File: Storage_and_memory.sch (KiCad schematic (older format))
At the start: 19 parts, among them J4 DM3AT-SF-PEJM5, U14 SN74AVCA406DGGR, U15 W25Q256JVFIQ

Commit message: minor changes
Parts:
- R19, R20, R21, R22: footprint Resistor_SMD:R_0805_2012Metric_Pad1.20x1.40mm_HandSolder -> Resistor_SMD:R_0805_2012Metric
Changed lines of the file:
@@
 F 0 "R19" V 4650 6430 50  0000 C CNN
 F 1 "33" V 4660 6810 50  0000 C CNN
-F 2 "Resistor_SMD:R_0805_2012Metric_Pad1.20x1.40mm_HandSolder" V 4630 6610 50  0001 C CNN
+F 2 "Resistor_SMD:R_0805_2012Metric" V 4630 6610 50  0001 C CNN
 F 3 "~" H 4700 6610 50  0001 C CNN
 F 4 "RC0805FR-0733RL" V 4700 6610 50  0001 C CNN "Type"
@@
 F 0 "R20" V 4660 6530 50  0000 C CNN
 F 1 "33" V 4660 6910 50  0000 C CNN
-F 2 "Resistor_SMD:R_0805_2012Metric_Pad1.20x1.40mm_HandSolder" V 4630 6710 50  0001 C CNN
+F 2 "Resistor_SMD:R_0805_2012Metric" V 4630 6710 50  0001 C CNN
 F 3 "~" H 4700 6710 50  0001 C CNN
 F 4 "RC0805FR-0733RL" V 4700 6710 50  0001 C CNN "Type"
@@
 F 0 "R21" V 4610 6830 50  0000 C CNN
 F 1 "33" V 4610 6970 50  0000 C CNN
-F 2 "Resistor_SMD:R_0805_2012Metric_Pad1.20x1.40mm_HandSolder" V 4630 6910 50  0001 C CNN
+F 2 "Resistor_SMD:R_0805_2012Metric" V 4630 6910 50  0001 C CNN
 F 3 "~" H 4700 6910 50  0001 C CNN
 F 4 "RC0805FR-0733RL" V 4700 6910 50  0001 C CNN "Type"
@@
 F 0 "R22" V 4790 6930 50  0000 C CNN
 F 1 "33" V 4790 7070 50  0000 C CNN
-F 2 "Resistor_SMD:R_0805_2012Metric_Pad1.20x1.40mm_HandSolder" V 4630 7010 50  0001 C CNN
+F 2 "Resistor_SMD:R_0805_2012Metric" V 4630 7010 50  0001 C CNN
 F 3 "~" H 4700 7010 50  0001 C CNN
 F 4 "RC0805FR-0733RL" V 4700 7010 50  0001 C CNN "Type"

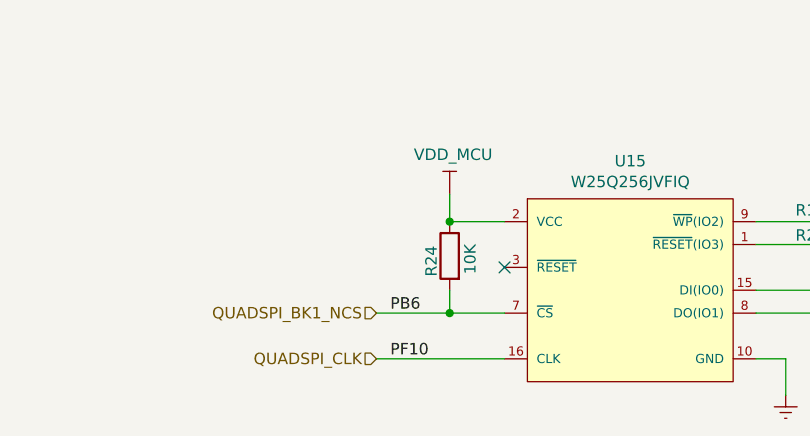
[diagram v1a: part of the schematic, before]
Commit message: NRST to QSPI Flash Reset pin has been connected
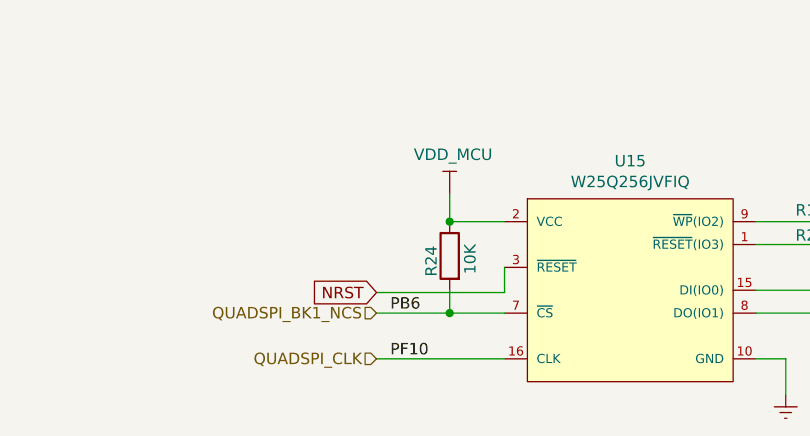
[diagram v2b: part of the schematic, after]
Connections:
- net NRST: now reaches U15.3 (~RESET)
- no-connect marks 10 -> 9
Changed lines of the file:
@@
 Wire Wire Line
 	4280 7010 4550 7010
-NoConn ~ 3180 6810
 Wire Wire Line
 	2620 7010 2940 7010
@@
 Wire Wire Line
 	2940 7010 3180 7010
+Wire Wire Line
+	3180 6810 3180 6920
+Wire Wire Line
+	3180 6920 2620 6920
+Text GLabel 2620 6920 0    50   Input ~ 0
+NRST
 $EndSCHEMATC

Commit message: commit after KiCAD library updates
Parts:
- U15: symbol Схема-и-печатная-плата-rescue:W25Q256JVFIQ-Memory_Flash -> Schema_and_PCB-rescue:W25Q256JVFIQ-Memory_Flash-Схема-и-печатная-плата-rescue
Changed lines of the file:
@@
 $EndDescr
 $Comp
-L Схема-и-печатная-плата-rescue:W25Q256JVFIQ-Memory_Flash U15
+L Schema_and_PCB-rescue:W25Q256JVFIQ-Memory_Flash-Схема-и-печатная-плата-rescue U15
 U 1 1 60D8B67A
 P 3180 6610
+AR Path="/60D8B67A" Ref="U15"  Part="1"
+AR Path="/60D8A641/60D8B67A" Ref="U15"  Part="1"
 F 0 "U15" H 3730 6875 50  0000 C CNN
 F 1 "W25Q256JVFIQ" H 3730 6784 50  0000 C CNN
